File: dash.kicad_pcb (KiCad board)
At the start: 2 copper layers, 48 x 70 mm, 24 parts, among them IC1 ATMEGA328-P, P1 JTAG, P2 ICSP, P3 ESP8266, P4 IN, P5 OUT, U1 LM317T, U2 TLC5916, Y1 16MHz

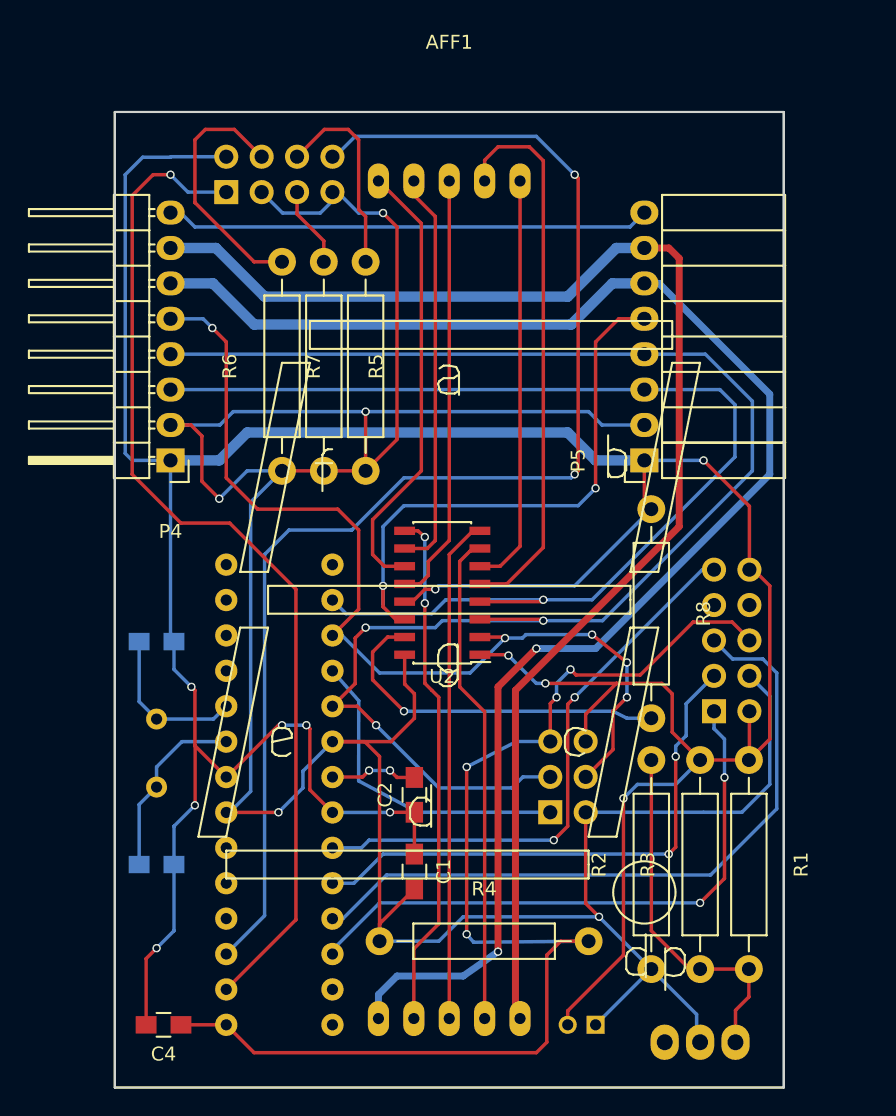
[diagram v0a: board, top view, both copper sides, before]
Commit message: Re-layout the PCB. vertical resistors, red/green supply mosfets.
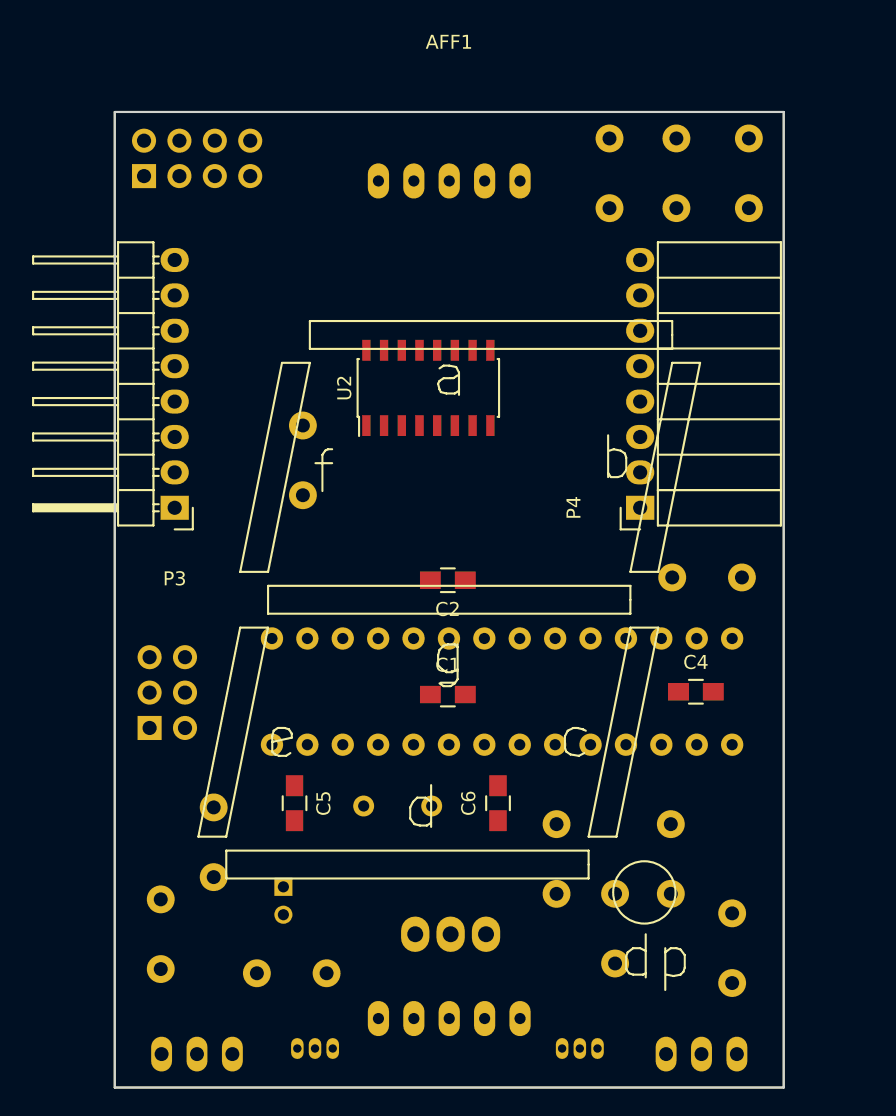
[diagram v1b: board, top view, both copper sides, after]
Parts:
- removed P5: OUT, Socket_Strips:Socket_Strip_Angled_1x08
- added Q1: Q_NPN_CBE, TO_SOT_Packages_THT:TO-92_Inline_Narrow_Oval, B.Cu at (137.6, 137.2)
- added Q2: Q_NPN_CBE, TO_SOT_Packages_THT:TO-92_Inline_Narrow_Oval, B.Cu at (156.6, 137.2)
- added Q3: Q_PMOS_GDS, TO_SOT_Packages_THT:TO-220_Neutral123_Vertical, B.Cu at (130.4, 137.6)
- added Q4: Q_PMOS_GDS, TO_SOT_Packages_THT:TO-220_Neutral123_Vertical, B.Cu at (166.6, 137.6)
- added R10: 4.7k, Resistors_ThroughHole:Resistor_Vertical_RM5mm, B.Cu at (164.4, 123.6)
- added R11: 10k, Resistors_ThroughHole:Resistor_Vertical_RM5mm, B.Cu at (127.8, 129.0)
- added R12: 10k, Resistors_ThroughHole:Resistor_Vertical_RM5mm, B.Cu at (168.8, 130.0)
- added R9: 4.7k, Resistors_ThroughHole:Resistor_Vertical_RM5mm, B.Cu at (131.6, 122.4)
- C5, C6: moved to F.Cu
- P1: value JTAG -> ICSP; footprint Pin_Headers:Pin_Header_Straight_2x05 -> Pin_Headers:Pin_Header_Straight_2x03
- P2: value ICSP -> ESP8266; footprint Pin_Headers:Pin_Header_Straight_2x03 -> Socket_Strips:Socket_Strip_Straight_2x04
- P3: value ESP8266 -> IN; footprint Socket_Strips:Socket_Strip_Straight_2x04 -> Pin_Headers:Pin_Header_Angled_1x08; moved to F.Cu
- P4: value IN -> OUT; footprint Pin_Headers:Pin_Header_Angled_1x08 -> Socket_Strips:Socket_Strip_Angled_1x08
- R1, R2, R3, R4, R5, R6, R7, R8: footprint Resistors_ThroughHole:Resistor_Horizontal_RM15mm -> Resistors_ThroughHole:Resistor_Vertical_RM5mm; moved to B.Cu
- moved P2 54.2 mm to (126.6, 74.6)
- moved C4 45.1 mm to (166.2, 111.6), turned to 0 degrees
- moved IC1 41.5 mm to (168.8, 115.4), turned to 90 degrees
- moved P1 40.5 mm to (127.0, 114.2)
- moved R6 39.7 mm to (170.0, 74.4)
- moved R4 35.1 mm to (167.0, 103.4)
- moved P4 33.9 mm to (162.2, 98.4), turned to 90 degrees
- moved R7 30.9 mm to (164.8, 74.4)
- moved R3 29.3 mm to (137.2, 131.8), turned to 180 degrees
- moved R8 25.2 mm to (138.0, 95.0), turned to 90 degrees
- moved C6 24.9 mm to (152.0, 119.6), turned to 90 degrees
- moved C3 24.5 mm to (136.6, 125.6), turned to 270 degrees
- moved P3 23.0 mm to (128.8, 98.4), turned to 180 degrees
- moved R5 21.5 mm to (160.0, 74.4)
- moved U1 19.5 mm to (148.6, 129.0), turned to 0 degrees
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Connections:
- AFF1 pad 1: Net-(AFF1-Pad1) -> PWR_RED
- AFF1 pad 5: Net-(AFF1-Pad5) -> PWR_GREEN
- IC1 pad 11: Net-(IC1-Pad11) -> (no net)
- IC1 pad 12: Net-(IC1-Pad12) -> (no net)
- IC1 pad 13: Net-(IC1-Pad13) -> (no net)
- IC1 pad 14: Net-(IC1-Pad14) -> (no net)
- IC1 pad 15: Net-(IC1-Pad15) -> (no net)
- IC1 pad 23: Net-(IC1-Pad23) -> (no net)
- IC1 pad 24: Net-(IC1-Pad24) -> (no net)
- IC1 pad 25: Net-(IC1-Pad25) -> (no net)
- IC1 pad 26: Net-(IC1-Pad26) -> (no net)
- IC1 pad 27: Net-(IC1-Pad27) -> (no net)
- IC1 pad 28: Net-(IC1-Pad28) -> (no net)
- IC1 pad 4: Net-(IC1-Pad4) -> EN_RED
- IC1 pad 5: Net-(IC1-Pad5) -> EN_GREEN
- IC1 pad 6: Net-(IC1-Pad6) -> (no net)
- P1 pad 1: Net-(IC1-Pad26) -> Net-(IC1-Pad18)
- P1 pad 2: GND -> VCC
- P1 pad 3: Net-(IC1-Pad24) -> Net-(IC1-Pad19)
- P1 pad 4: VCC -> Net-(IC1-Pad17)
- P1 pad 5: Net-(IC1-Pad25) -> Net-(C4-Pad1)
- P1 pad 6: Net-(C4-Pad1) -> GND
- P2 pad 1: Net-(IC1-Pad18) -> Net-(IC1-Pad2)
- P2 pad 2: VCC -> GND
- P2 pad 3: Net-(IC1-Pad19) -> VCC
- P2 pad 4: Net-(IC1-Pad17) -> Net-(P2-Pad4)
- P2 pad 5: Net-(C4-Pad1) -> Net-(P2-Pad5)
- P2 pad 6: GND -> Net-(P2-Pad6)
- P3 pad 1: Net-(IC1-Pad2) -> GND
- P3 pad 2: GND -> VCC
- P3 pad 3: VCC -> Net-(IC1-Pad16)
- P3 pad 4: Net-(P3-Pad4) -> Net-(IC1-Pad19)
- P3 pad 5: Net-(P3-Pad5) -> Net-(IC1-Pad17)
- P3 pad 6: Net-(P3-Pad6) -> PWR_RED
- P3 pad 7: VCC -> PWR_GREEN
- P3 pad 8: Net-(IC1-Pad3) -> Net-(P3-Pad8)
- P4 pad 5: Net-(IC1-Pad17) -> Net-(P4-Pad5)
- P4 pad 6: Net-(AFF1-Pad1) -> PWR_RED
- P4 pad 7: Net-(AFF1-Pad5) -> PWR_GREEN
- P4 pad 8: Net-(P4-Pad8) -> Net-(P3-Pad8)
- R5 pad 1: Net-(P3-Pad5) -> Net-(P2-Pad5)
- R6 pad 2: Net-(P3-Pad4) -> Net-(P2-Pad4)
- R7 pad 2: Net-(P3-Pad6) -> Net-(P2-Pad6)
- U2 pad 14: Net-(P5-Pad5) -> Net-(P4-Pad5)
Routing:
- net GND: track 245.8 -> 0.00 mm, vias 11 -> 0
- net VCC: track 223.2 -> 0.00 mm, vias 5 -> 0
- net Net-(AFF1-Pad1): track 110.7 -> 0.00 mm, vias 2 -> 0
- net Net-(IC1-Pad19): track 110.2 -> 0.00 mm, vias 3 -> 0
- net Net-(AFF1-Pad5): track 99.3 -> 0.00 mm
- net Net-(IC1-Pad3): track 95.3 -> 0.00 mm, vias 2 -> 0
- net Net-(C4-Pad1): track 85.5 -> 0.00 mm, vias 4 -> 0
- net Net-(IC1-Pad16): track 83.2 -> 0.00 mm, vias 1 -> 0
- net Net-(IC1-Pad2): track 73.8 -> 0.00 mm, vias 1 -> 0
- net Net-(IC1-Pad17): track 69.2 -> 0.00 mm, vias 5 -> 0
- net Net-(IC1-Pad25): track 50.4 -> 0.00 mm
- net Net-(IC1-Pad26): track 42.9 -> 0.00 mm, vias 2 -> 0
- net Net-(IC1-Pad23): track 40.8 -> 0.00 mm, vias 2 -> 0
- net Net-(P5-Pad5): track 40.0 -> 0.00 mm, vias 2 -> 0
- net Net-(AFF1-Pad7): track 39.9 -> 0.00 mm
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
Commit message: Start re-routing new layout.
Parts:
- added P5: DC, Pin_Headers:Pin_Header_Straight_1x02, F.Cu at (170.6, 128.2)
- moved P3 39.7 mm to (168.3, 102.7), turned to 0 degrees
- moved P4 27.7 mm to (134.8, 102.7), turned to 270 degrees
- moved R2 26.0 mm to (159.0, 97.8), turned to 0 degrees
- moved R8 23.5 mm to (159.1, 105.3), turned to 270 degrees
- moved IC1 22.6 mm to (169.8, 92.8)
- moved P1 22.6 mm to (126.6, 91.6)
- moved C1 22.6 mm to (148.6, 89.2)
- moved C2 22.6 mm to (148.6, 81.0)
- moved C4 22.6 mm to (166.4, 89.0)
- moved C5 22.6 mm to (137.6, 97.0)
- moved C6 22.6 mm to (152.2, 97.0)
- moved Y1 22.6 mm to (145.0, 97.2)
- moved R4 22.4 mm to (167.2, 81.0)
- moved U2 20.0 mm to (151.3, 109.3)
- moved C3 12.4 mm to (148.6, 122.4), turned to 180 degrees
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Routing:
- net GND: track 0.00 -> 91.2 mm, vias 0 -> 2
- net PWR_RED: track 0.00 -> 80.1 mm
- net PWR_GREEN: track 0.00 -> 74.8 mm
- net +12V: track 0.00 -> 62.3 mm
- net Net-(Q2-Pad1): track 0.00 -> 29.8 mm
- net Net-(Q1-Pad1): track 0.00 -> 19.0 mm
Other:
- outline, holes or cut-outs redrawn

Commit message: Finish routing second attempt.
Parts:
- moved P2 35.6 mm to (162.2, 75.8)
- moved R4 30.8 mm to (137.0, 74.8), turned to 90 degrees
- moved P1 12.2 mm to (128.6, 79.6)
- moved R6 11.9 mm to (158.8, 78.4)
- moved C2 10.3 mm to (154.8, 89.2)
- moved R5 9.88 mm to (168.0, 80.2), turned to 0 degrees
- moved R7 8.68 mm to (156.2, 75.6)
- moved Q2 2.60 mm to (158.8, 136.6), turned to 180 degrees
- moved C4 1.02 mm to (165.4, 89.2), turned to 180 degrees
- moved R1 0.20 mm to (156.4, 127.2)
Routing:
- net VCC: track 0.00 -> 157.3 mm, vias 0 -> 4
- net GND: track 91.2 -> 240.7 mm, vias 2 -> 3
- net Net-(AFF1-Pad6): track 0.00 -> 114.5 mm, vias 0 -> 1
- net Net-(IC1-Pad19): track 0.00 -> 113.5 mm, vias 0 -> 4
- net Net-(AFF1-Pad7): track 0.00 -> 105.8 mm, vias 0 -> 3
- net Net-(IC1-Pad17): track 0.00 -> 94.8 mm, vias 0 -> 4
- net Net-(IC1-Pad16): track 0.00 -> 67.4 mm, vias 0 -> 3
- net Net-(C4-Pad1): track 0.00 -> 66.0 mm, vias 0 -> 2
- net EN_RED: track 0.00 -> 62.3 mm, vias 0 -> 1
- net Net-(R1-Pad2): track 0.00 -> 61.1 mm, vias 0 -> 4
- net Net-(AFF1-Pad9): track 0.00 -> 61.0 mm, vias 0 -> 2
- net Net-(AFF1-Pad10): track 0.00 -> 58.5 mm, vias 0 -> 2
- net Net-(AFF1-Pad2): track 0.00 -> 44.5 mm
- net Net-(AFF1-Pad8): track 0.00 -> 42.6 mm
- net Net-(P3-Pad8): track 0.00 -> 34.2 mm
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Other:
- outline, holes or cut-outs redrawn

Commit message: Re-orient the ESP8266 header.
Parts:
- added github.com/jimmo/counter-dash: github.com/jimmo/counter-dash, Symbols:Symbol_OSHW-Logo_SilkScreen, B.Cu at (153.3, 114.8)
- moved R5 1.79 mm to (166.4, 81.0)
- moved P2 0.45 mm to (162.4, 75.4)
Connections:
- P2 pad 1: Net-(IC1-Pad2) -> VCC
- P2 pad 2: GND -> Net-(IC1-Pad3)
- P2 pad 3: VCC -> Net-(P2-Pad3)
- P2 pad 5: Net-(P2-Pad5) -> VCC
- P2 pad 7: VCC -> Net-(IC1-Pad2)
- P2 pad 8: Net-(IC1-Pad3) -> GND
- R5 pad 1: Net-(P2-Pad5) -> Net-(P2-Pad3)
- R6 pad 2: Net-(P2-Pad4) -> Net-(P2-Pad6)
- R7 pad 2: Net-(P2-Pad6) -> Net-(P2-Pad4)
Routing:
- net GND: track 240.7 -> 254.6 mm
- net Net-(P2-Pad3): track 0.00 -> 6.03 mm
- net Net-(P2-Pad5): track 5.14 -> 0.00 mm
- net VCC: track 157.3 -> 162.3 mm
- net Net-(IC1-Pad2): track 26.3 -> 22.5 mm
- net Net-(C4-Pad1): track 66.0 -> 67.4 mm
- net Net-(P2-Pad4): track 9.94 -> 11.1 mm
- net Net-(P2-Pad6): track 13.5 -> 12.5 mm
- net Net-(IC1-Pad3): track 22.8 -> 23.3 mm

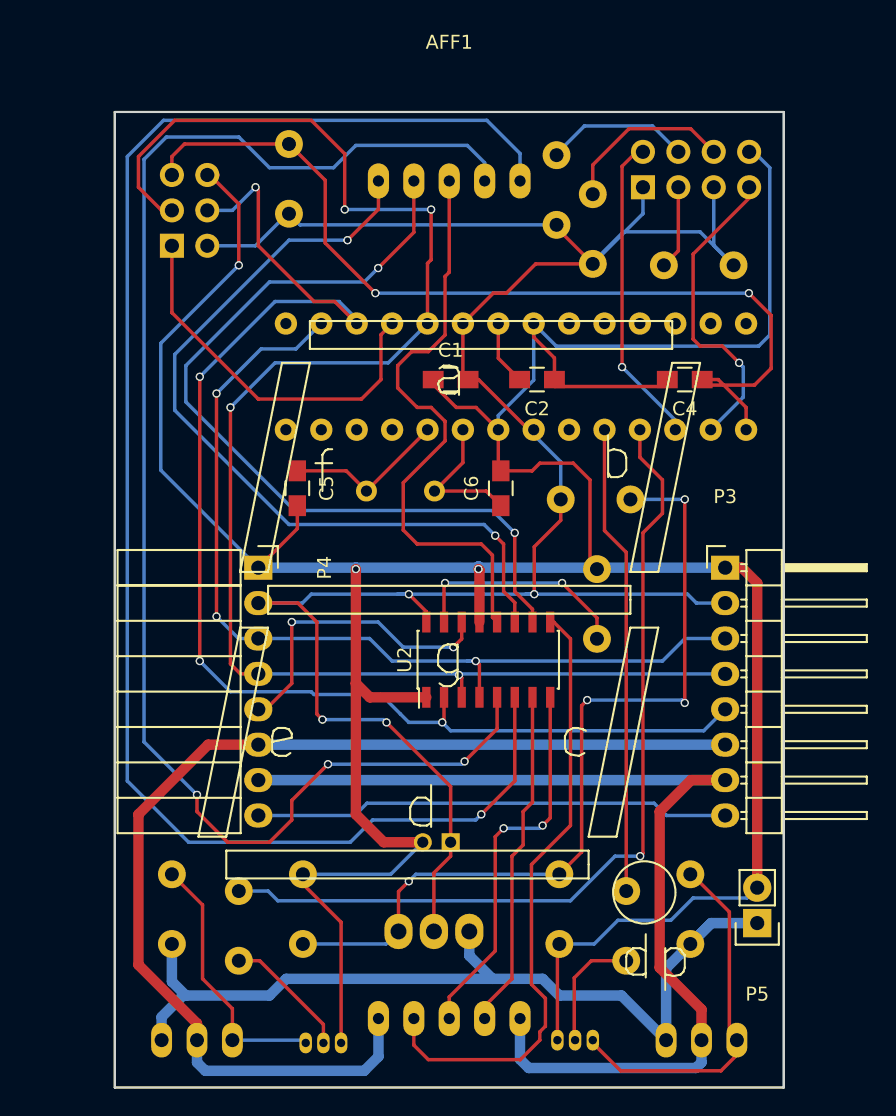
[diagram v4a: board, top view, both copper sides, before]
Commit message: Change vias to 0.3mm
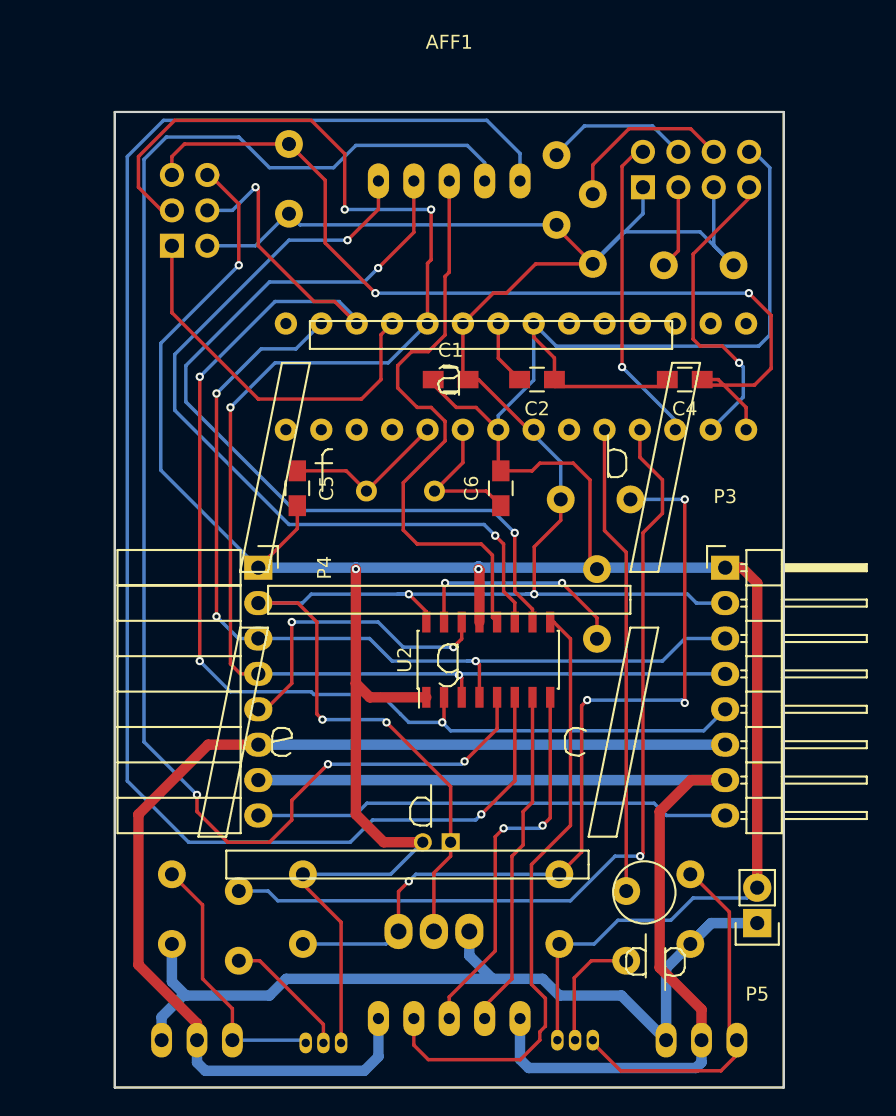
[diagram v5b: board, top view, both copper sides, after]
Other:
- net class Default: via_drill 0.4 -> 0.3
- net class High Current: via_drill 0.4 -> 0.3
